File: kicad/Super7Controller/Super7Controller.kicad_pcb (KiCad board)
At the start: 2 copper layers, 49.5 x 25.4 mm, 20 parts, among them P3 CONN_01X13, P4 CONN_01X09, U1 ULN2003A, U2 HiLetgo_ESP-WROOM-32_Developm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

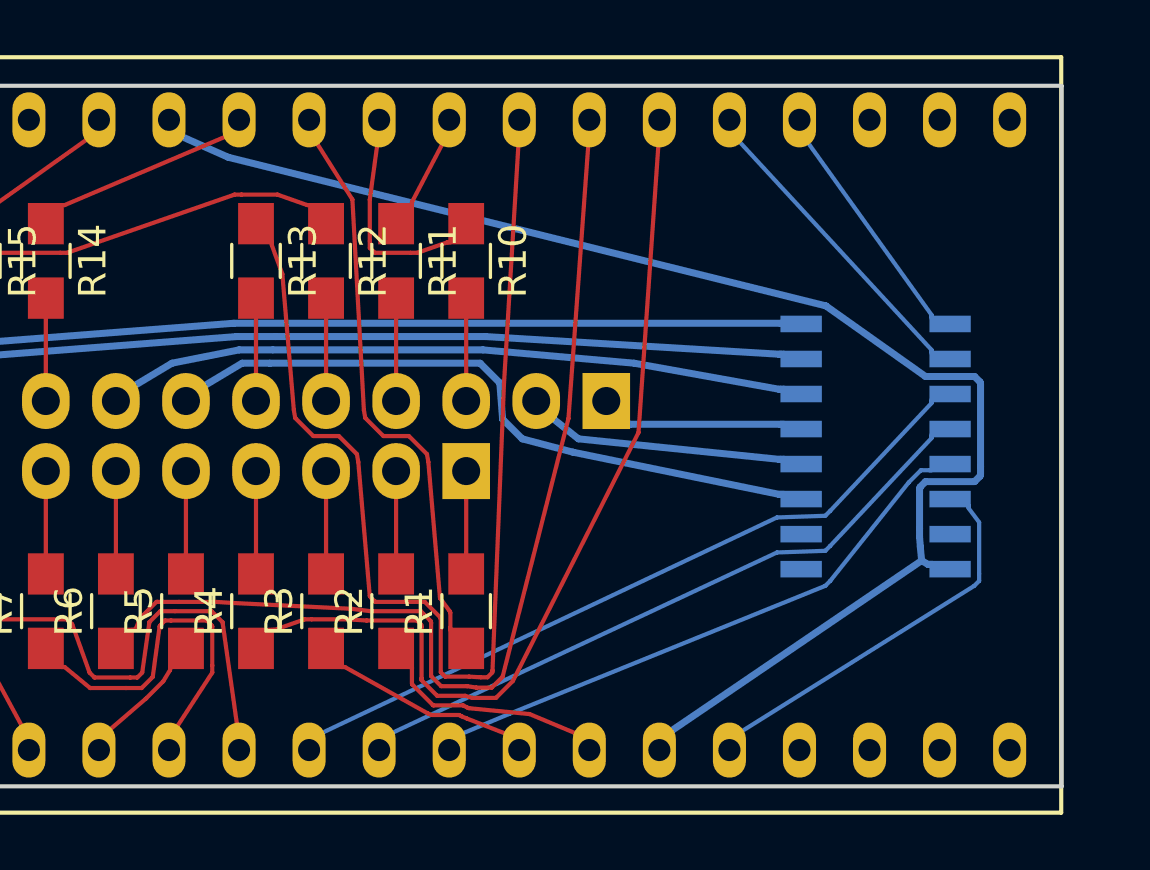
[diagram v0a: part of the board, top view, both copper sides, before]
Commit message: replace long ground trace with something shorter
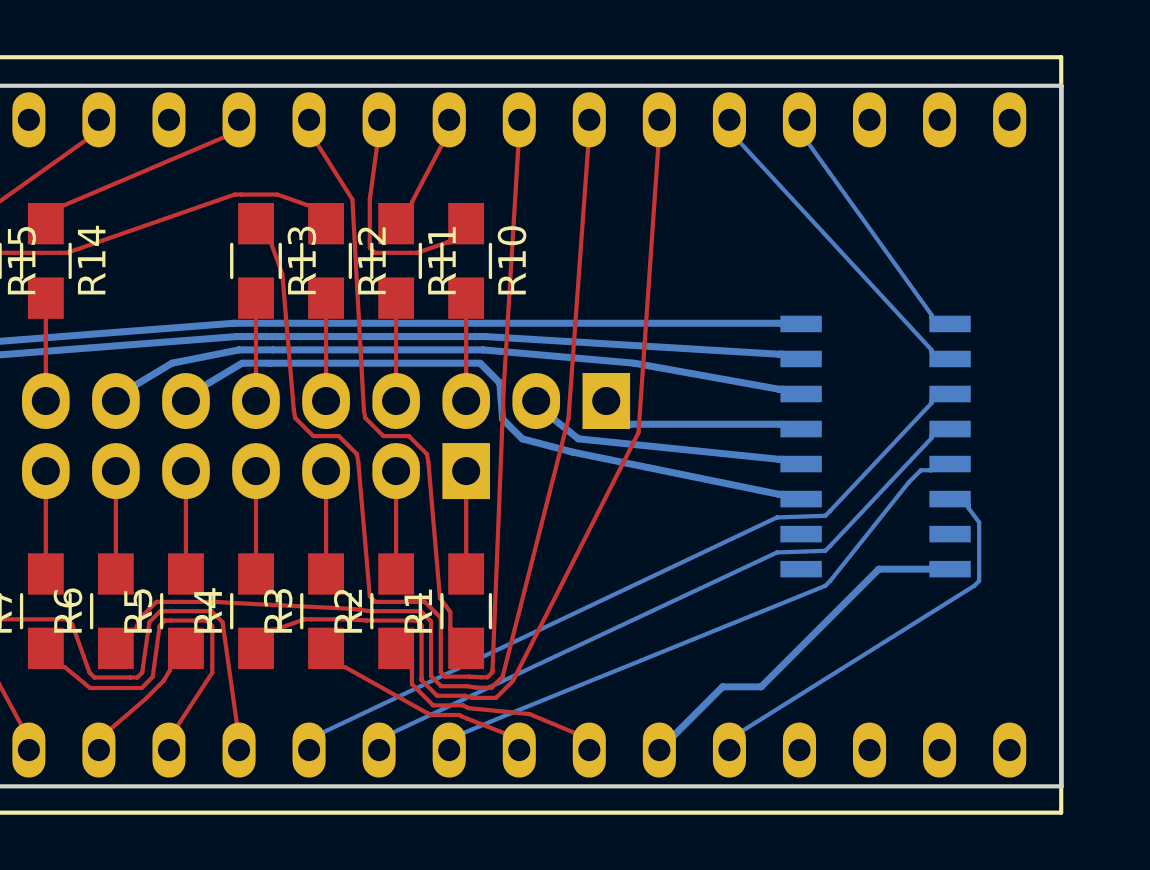
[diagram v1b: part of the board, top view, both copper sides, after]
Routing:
- net GND: track 50.2 -> 13.9 mm
- net Net-(U2-Pad32): track 2.75 -> 0.40 mm
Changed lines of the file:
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@@
     (thickness 1.6)
     (drawings 10)
-    (tracks 381)
+    (tracks 363)
     (zones 0)
     (modules 20)
@@
   )
   (gr_line (start 69.215 53.34) (end 69.215 78.74) (angle 90) (layer Edge.Cuts) (width 0.15))
-  (segment (start 104.16 77.025) (end 113.6681 70.5566) (width 0.254) (layer B.Cu) (net 1))
-  (segment (start 104.16 77.425) (end 104.16 77.025) (width 0.254) (layer B.Cu) (net 1))
+  (segment (start 114.7 70.866) (end 112.1156 70.866) (width 0.254) (layer B.Cu) (net 1) (status 400000))
+  (segment (start 106.4518 75.1332) (end 104.16 77.425) (width 0.254) (layer B.Cu) (net 1) (status 800000))
+  (segment (start 107.8484 75.1332) (end 106.4518 75.1332) (width 0.254) (layer B.Cu) (net 1))
+  (segment (start 112.1156 70.866) (end 107.8484 75.1332) (width 0.254) (layer B.Cu) (net 1))
   (segment (start 114.077 70.693) (end 114.7 70.866) (width 0.254) (layer B.Cu) (net 1))
-  (segment (start 113.95 70.693) (end 114.077 70.693) (width 0.254) (layer B.Cu) (net 1))
-  (segment (start 113.8974 70.693) (end 113.95 70.693) (width 0.254) (layer B.Cu) (net 1))
-  (segment (start 113.6681 70.5566) (end 113.8974 70.693) (width 0.254) (layer B.Cu) (net 1))
-  (segment (start 113.6199 70.0433) (end 113.6681 70.5566) (width 0.254) (layer B.Cu) (net 1))
-  (segment (start 113.5943 69.694) (end 113.6199 70.0433) (width 0.254) (layer B.Cu) (net 1))
-  (segment (start 113.5943 69.3994) (end 113.5943 69.694) (width 0.254) (layer B.Cu) (net 1))
-  (segment (start 113.5943 67.9549) (end 113.5943 69.3994) (width 0.254) (layer B.Cu) (net 1))
-  (segment (start 113.615 67.8872) (end 113.5943 67.9549) (width 0.254) (layer B.Cu) (net 1))
-  (segment (start 113.8112 67.691) (end 113.615 67.8872) (width 0.254) (layer B.Cu) (net 1))
-  (segment (start 115.5888 67.691) (end 113.8112 67.691) (width 0.254) (layer B.Cu) (net 1))
-  (segment (start 115.785 67.4948) (end 115.5888 67.691) (width 0.254) (layer B.Cu) (net 1))
-  (segment (start 115.8057 67.4271) (end 115.785 67.4948) (width 0.254) (layer B.Cu) (net 1))
-  (segment (start 115.8057 67.1325) (end 115.8057 67.4271) (width 0.254) (layer B.Cu) (net 1))
-  (segment (start 115.8057 64.1449) (end 115.8057 67.1325) (width 0.254) (layer B.Cu) (net 1))
-  (segment (start 115.785 64.0772) (end 115.8057 64.1449) (width 0.254) (layer B.Cu) (net 1))
-  (segment (start 115.5888 63.881) (end 115.785 64.0772) (width 0.254) (layer B.Cu) (net 1))
-  (segment (start 113.8112 63.881) (end 115.5888 63.881) (width 0.254) (layer B.Cu) (net 1))
-  (segment (start 110.1973 61.3203) (end 113.8112 63.881) (width 0.254) (layer B.Cu) (net 1))
-  (segment (start 88.5241 55.9307) (end 110.1973 61.3203) (width 0.254) (layer B.Cu) (net 1))
   (segment (start 102.9716 65.613) (end 102.235 64.77) (width 0.254) (layer B.Cu) (net 3))
   (segment (start 103.0986 65.613) (end 102.9716 65.613) (width 0.254) (layer B.Cu) (net 3))
@@
   (segment (start 115.3738 68.5498) (end 115.3738 68.626) (width 0.1524) (layer B.Cu) (net 61))
   (segment (start 114.7 68.326) (end 115.3738 68.5498) (width 0.1524) (layer B.Cu) (net 61))
-  (segment (start 86.38 54.975) (end 88.5241 55.9307) (width 0.254) (layer B.Cu) (net 62))
   (segment (start 86.38 54.575) (end 86.38 54.975) (width 0.254) (layer B.Cu) (net 62))
 )

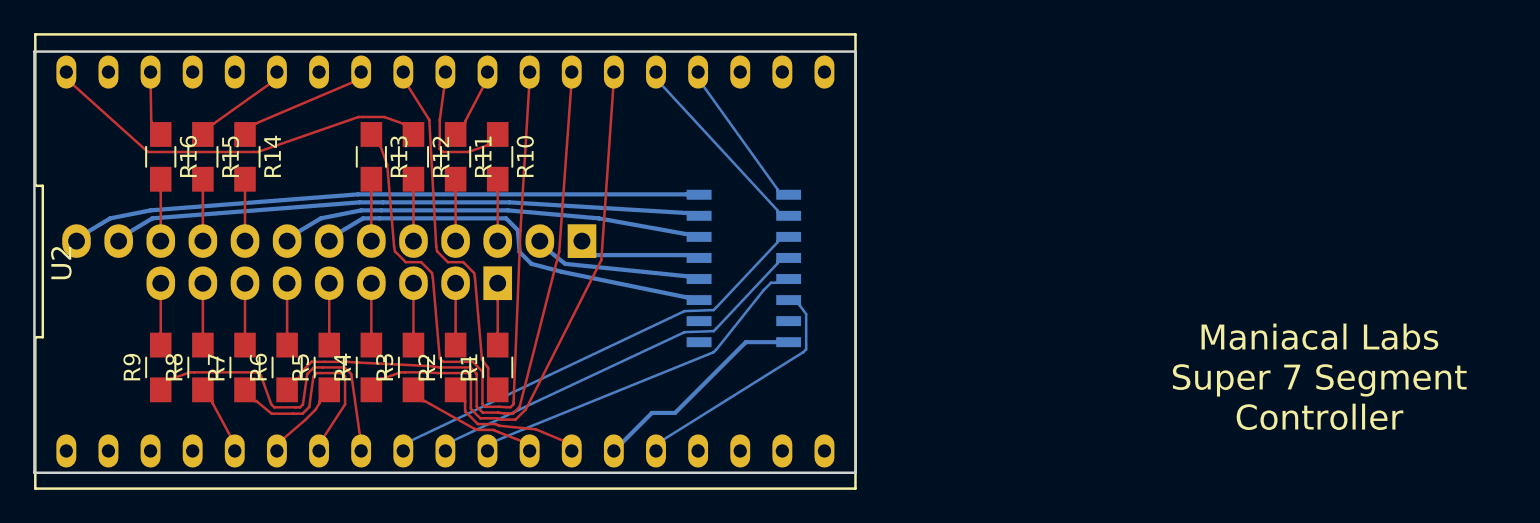
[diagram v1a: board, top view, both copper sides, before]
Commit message: export netlist into layout and remove already routed lines
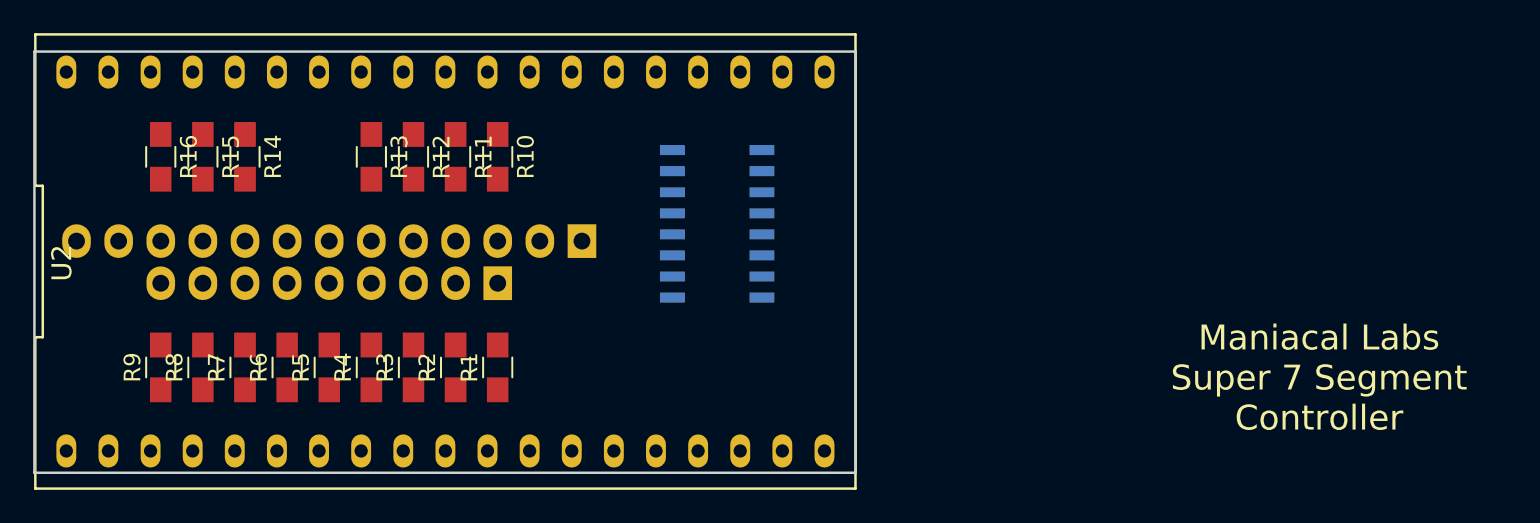
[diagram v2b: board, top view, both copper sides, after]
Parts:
- moved U1 3.14 mm to (110.4, 63.7)
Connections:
- U1 pad 11: DC_3 -> DC_1
- U1 pad 13: DC_1 -> DC_3
- U1 pad 4: DCD_1 -> DCD_3
- U1 pad 6: DCD_3 -> DCD_1
- U2 pad 10: DCD_1 -> Net-(R4-Pad1)
- U2 pad 11: DCD_2 -> Net-(R3-Pad1)
- U2 pad 12: Net-(R3-Pad1) -> Net-(R2-Pad1)
- U2 pad 13: Net-(R2-Pad1) -> Net-(R1-Pad1)
- U2 pad 15: DCD_3 -> DCD_1
- U2 pad 23: DCD_6 -> DCD_2
- U2 pad 24: DCD_5 -> DCD_3
- U2 pad 25: Net-(R4-Pad1) -> DCD_4
- U2 pad 26: Net-(R6-Pad1) -> DCD_5
- U2 pad 27: Net-(R13-Pad1) -> DCD_6
- U2 pad 28: Net-(R11-Pad1) -> Net-(R10-Pad1)
- U2 pad 29: Net-(R10-Pad1) -> Net-(R11-Pad1)
- U2 pad 30: Net-(R1-Pad1) -> Net-(R12-Pad1)
- U2 pad 31: Net-(R14-Pad1) -> Net-(R13-Pad1)
- U2 pad 33: Net-(R15-Pad1) -> Net-(R14-Pad1)
- U2 pad 36: Net-(R16-Pad1) -> Net-(R15-Pad1)
- U2 pad 37: (no net) -> Net-(R16-Pad1)
- U2 pad 38: Net-(R12-Pad1) -> Net-(U2-Pad38)
- U2 pad 5: Net-(R8-Pad1) -> Net-(R9-Pad1)
- U2 pad 6: Net-(R5-Pad1) -> Net-(R8-Pad1)
- U2 pad 8: Net-(R9-Pad1) -> Net-(R6-Pad1)
- U2 pad 9: DCD_4 -> Net-(R5-Pad1)
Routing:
- net Net-(R13-Pad1): track 42.2 -> 0.00 mm
- net DC_6: track 38.1 -> 0.00 mm
- net Net-(R6-Pad1): track 37.8 -> 0.00 mm
- net DC_5: track 35.6 -> 0.00 mm
- net Net-(R4-Pad1): track 33.7 -> 0.00 mm
- net DCD_4: track 27.4 -> 0.00 mm
- net DC_4: track 25.5 -> 0.00 mm
- net DC_3: track 24.8 -> 0.00 mm
- net DCD_1: track 24.5 -> 0.00 mm
- net Net-(R12-Pad1): track 23.8 -> 0.00 mm
- net DCD_2: track 21.7 -> 0.00 mm
- net Net-(R1-Pad1): track 21.5 -> 0.00 mm
- net Net-(R9-Pad1): track 19.9 -> 0.00 mm
- net DCD_3: track 14.7 -> 0.00 mm
- net GND: track 13.9 -> 0.00 mm
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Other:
- board text removed: "ULN2003A"

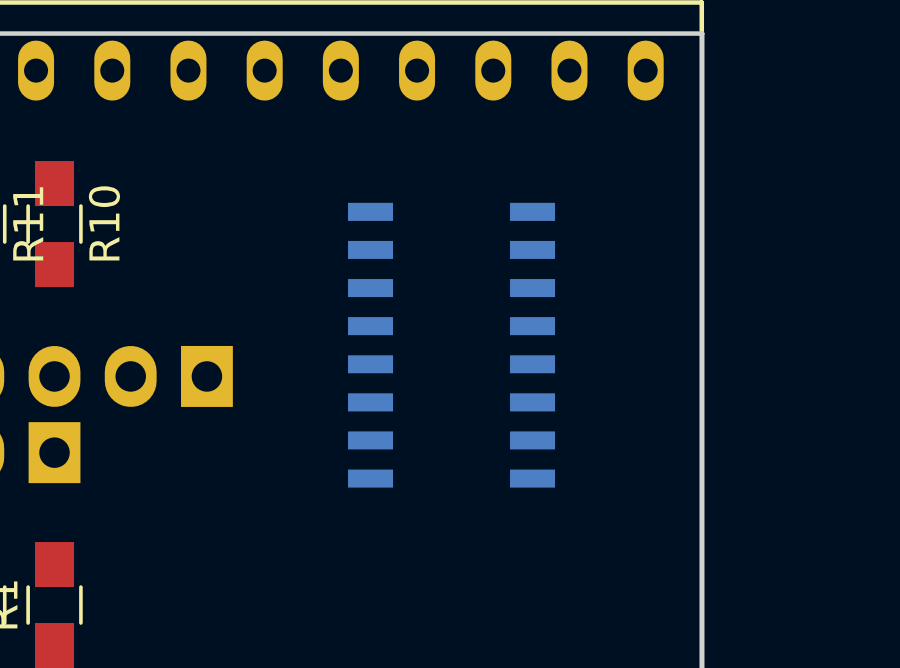
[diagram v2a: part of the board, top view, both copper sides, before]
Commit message: move the ULN up a little
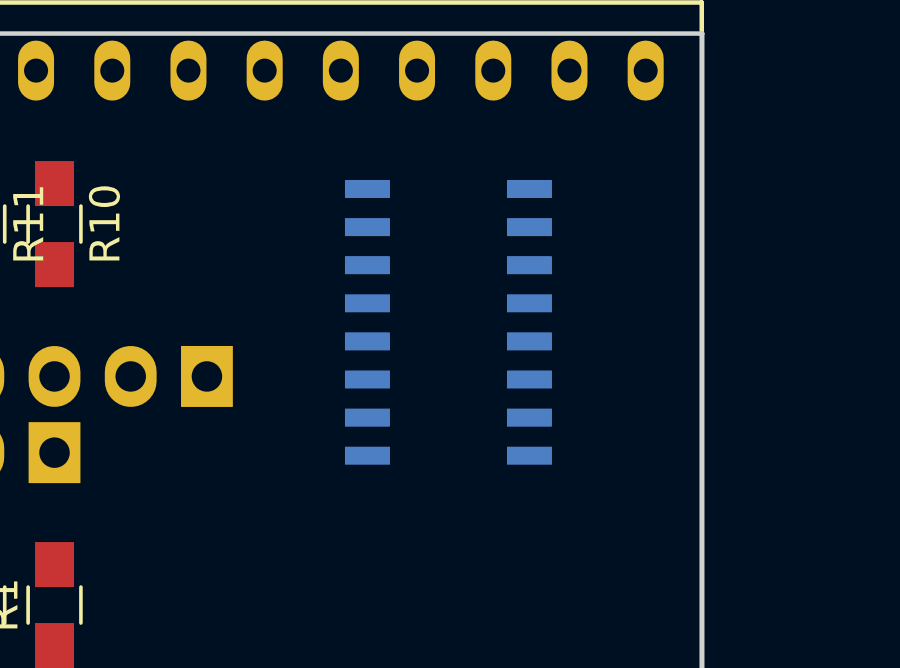
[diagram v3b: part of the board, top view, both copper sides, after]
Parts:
- moved U1 0.77 mm to (110.3, 63.0)
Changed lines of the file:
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@@
   )
   (module Housings_SOIC:SOIC-16_3.9x9.9mm_Pitch1.27mm (layer B.Cu)
-    (at 110.3884 63.7286 180)
+    (at 110.2868 62.9666 180)
     (descr "16-Lead Plastic Small Outline (SL) - Narrow, 3.90 mm Body [SOIC] (see Microchip Packaging Specification 00000049BS.pdf)")
     (tags "SOIC 1.27")

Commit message: 2 to 6 is better
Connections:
- U2 pad 23: DCD_2 -> DCD_6
- U2 pad 24: DCD_3 -> DCD_5
- U2 pad 26: DCD_5 -> DCD_3
- U2 pad 27: DCD_6 -> DCD_2
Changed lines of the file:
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@@
     (area 69.139999 53.264999 118.820001 78.815001)
     (thickness 1.6)
-    (drawings 9)
+    (drawings 8)
     (tracks 0)
     (zones 0)
@@
       (net 29 "Net-(R3-Pad1)"))
     (pad 27 thru_hole oval (at 5.08 -11.425) (size 1.2 2) (drill 0.8) (layers *.Cu *.Mask)
-      (net 56 DCD_6))
+      (net 60 DCD_2))
     (pad 12 thru_hole oval (at 5.08 11.425) (size 1.2 2) (drill 0.8) (layers *.Cu *.Mask)
       (net 28 "Net-(R2-Pad1)"))
     (pad 26 thru_hole oval (at 7.62 -11.425) (size 1.2 2) (drill 0.8) (layers *.Cu *.Mask)
-      (net 57 DCD_5))
+      (net 61 DCD_3))
     (pad 13 thru_hole oval (at 7.62 11.425) (size 1.2 2) (drill 0.8) (layers *.Cu *.Mask)
       (net 27 "Net-(R1-Pad1)"))
@@
       (net 1 GND))
     (pad 24 thru_hole oval (at 12.7 -11.425) (size 1.2 2) (drill 0.8) (layers *.Cu *.Mask)
-      (net 61 DCD_3))
+      (net 57 DCD_5))
     (pad 15 thru_hole oval (at 12.7 11.425) (size 1.2 2) (drill 0.8) (layers *.Cu *.Mask)
       (net 59 DCD_1))
     (pad 23 thru_hole oval (at 15.24 -11.425) (size 1.2 2) (drill 0.8) (layers *.Cu *.Mask)
-      (net 60 DCD_2))
+      (net 56 DCD_6))
     (pad 16 thru_hole oval (at 15.24 11.425) (size 1.2 2) (drill 0.8) (layers *.Cu *.Mask)
       (net 49 "Net-(U2-Pad16)"))
@@
   )
   (dimension 49.53 (width 0.3) (layer F.Fab)
-    (gr_text "1.9500 in" (at 93.98 49.45) (layer F.Fab)
-      (effects (font (size 1.5 1.5) (thickness 0.3)))
-    )
-    (feature1 (pts (xy 118.745 53.34) (xy 118.745 48.1)))
-    (feature2 (pts (xy 69.215 53.34) (xy 69.215 48.1)))
-    (crossbar (pts (xy 69.215 50.8) (xy 118.745 50.8)))
-    (arrow1a (pts (xy 118.745 50.8) (xy 117.618496 51.386421)))
-    (arrow1b (pts (xy 118.745 50.8) (xy 117.618496 50.213579)))
-    (arrow2a (pts (xy 69.215 50.8) (xy 70.341504 51.386421)))
-    (arrow2b (pts (xy 69.215 50.8) (xy 70.341504 50.213579)))
-  )
-  (dimension 49.53 (width 0.3) (layer F.Fab)

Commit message: Autoroute it and put it back into KiCad
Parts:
- moved U1 2.29 mm to (108.0, 62.9)
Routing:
- net DC_6: track 0.00 -> 34.4 mm
- net DC_5: track 0.00 -> 31.7 mm
- net DC_4: track 0.00 -> 21.5 mm
- net DC_3: track 0.00 -> 18.8 mm
- net DCD_2: track 0.00 -> 15.5 mm
- net DCD_1: track 0.00 -> 14.5 mm
- net DCD_3: track 0.00 -> 12.3 mm
- net GND: track 0.00 -> 12.3 mm
- net DCD_4: track 0.00 -> 9.39 mm
- net DCD_5: track 0.00 -> 6.75 mm
- net DC_2: track 0.00 -> 6.20 mm
- net Net-(R3-Pad1): track 0.00 -> 5.99 mm
- net Net-(R9-Pad1): track 0.00 -> 5.99 mm
- net Net-(R8-Pad1): track 0.00 -> 5.99 mm
- net Net-(R6-Pad1): track 0.00 -> 5.99 mm
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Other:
- board text added: "Maniacal Labs Super 7 Segment Controller Modified by Dillon Nichols tinkerer.us"
- board text removed: "Maniacal Labs Super 7 Segment Controller"

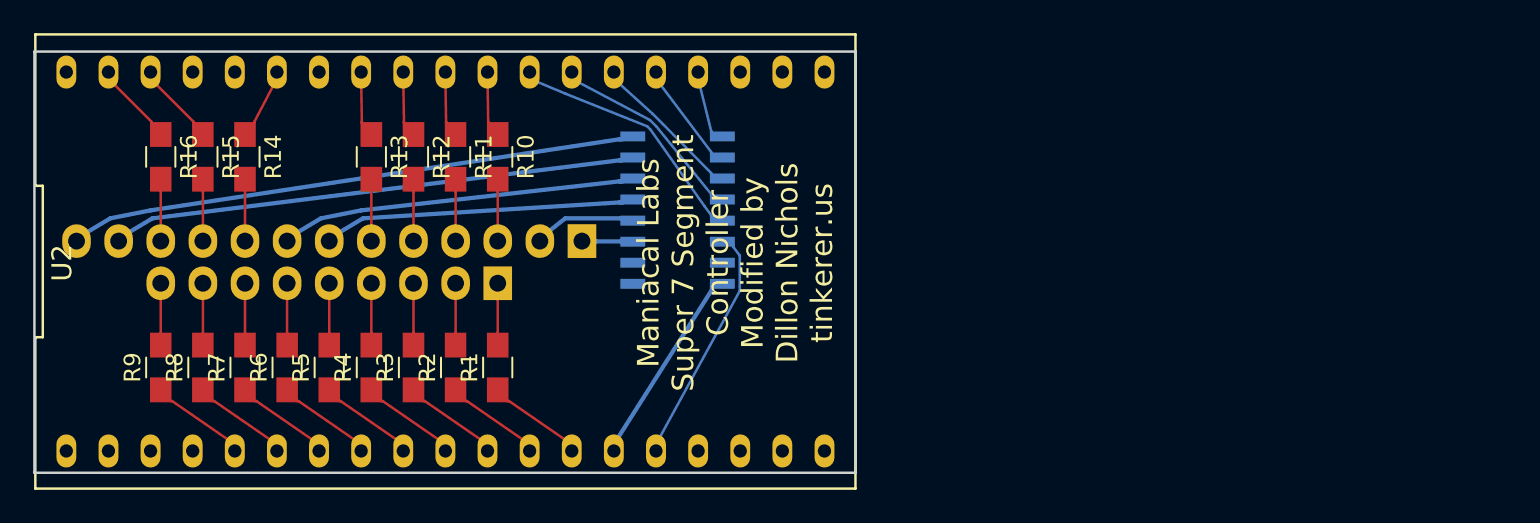
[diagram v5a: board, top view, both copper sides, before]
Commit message: remove/hide top layer silkscreen
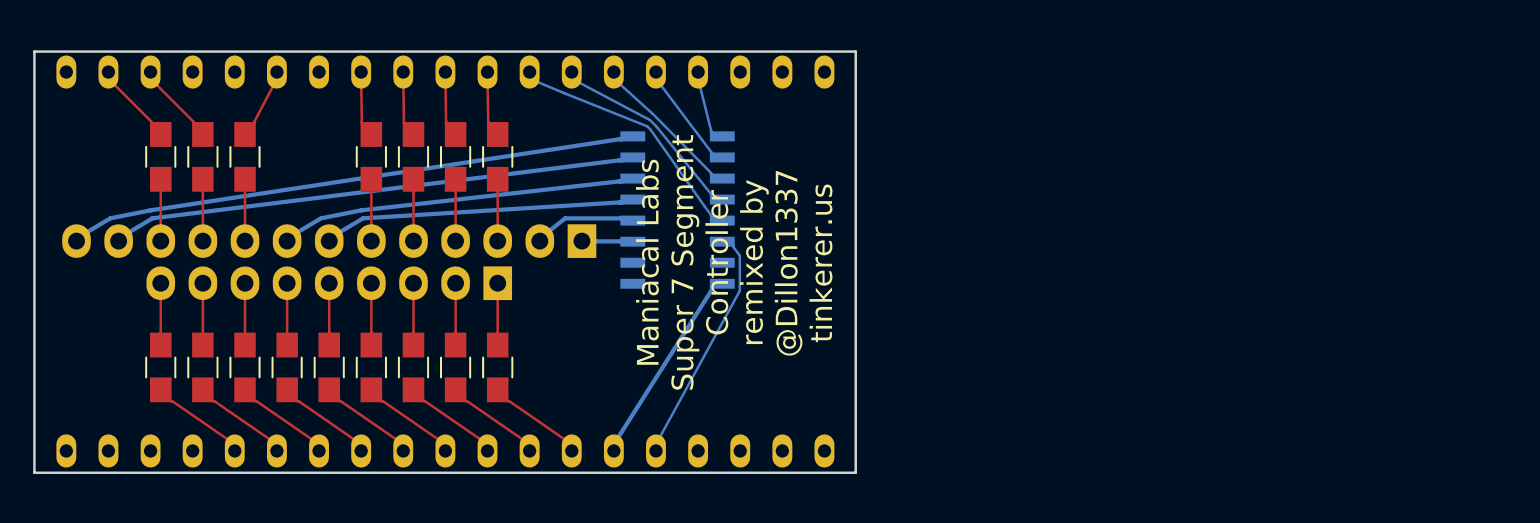
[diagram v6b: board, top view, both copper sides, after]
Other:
- board text added: "Maniacal Labs Super 7 Segment Controller remixed by @Dillon1337 tinkerer.us"
- board text removed: "Maniacal Labs Super 7 Segment Controller Modified by Dillon Nichols tinkerer.us"
